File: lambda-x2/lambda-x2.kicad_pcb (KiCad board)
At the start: 4 copper layers, 81.8 x 100.9 mm, 263 parts, among them J1 FTSH-107-01-F-DV-K, J3 Conn_02x02_Odd_Even, J4 Conn_01x10, P1 33311-24AW-2, Q1 BTS3028, Q2 BTS3028, Q3 BTS3028, Q4 BTS3028, U1 MAX31855KASA, U10 MCP6002T-I/SN, U11 GS8332-SR, U12 MCP6002T-I/SN, U13 MCP6002T-I/SN, U14 MAX31855KASA, U15 MAX31856, U16 MAX31856, U17 MCP6002T-I/SN, U18 JDY-33, U2 STM32F103C6Tx, U3 MCP6002T-I/SN, U4 LM78M05_TO252, U5 XC6206P332MR, U6 REF3033, U7 MCP6002T-I/SN, U8 TJA1051T-3, U9 GS8332-SR, Y1 XXDCELNANF-8MHZ

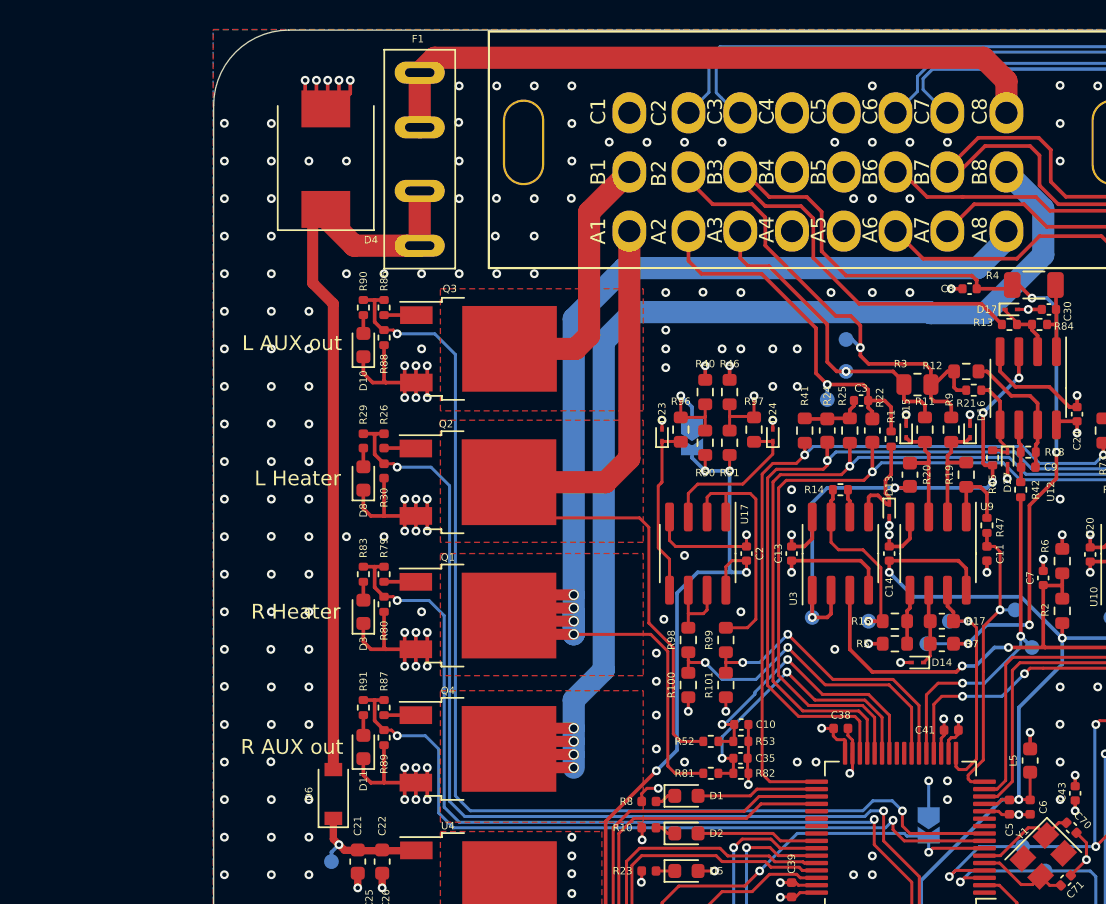
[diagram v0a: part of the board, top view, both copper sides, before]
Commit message: lambda-x2: fuse, Vbat sense, resistor in sense
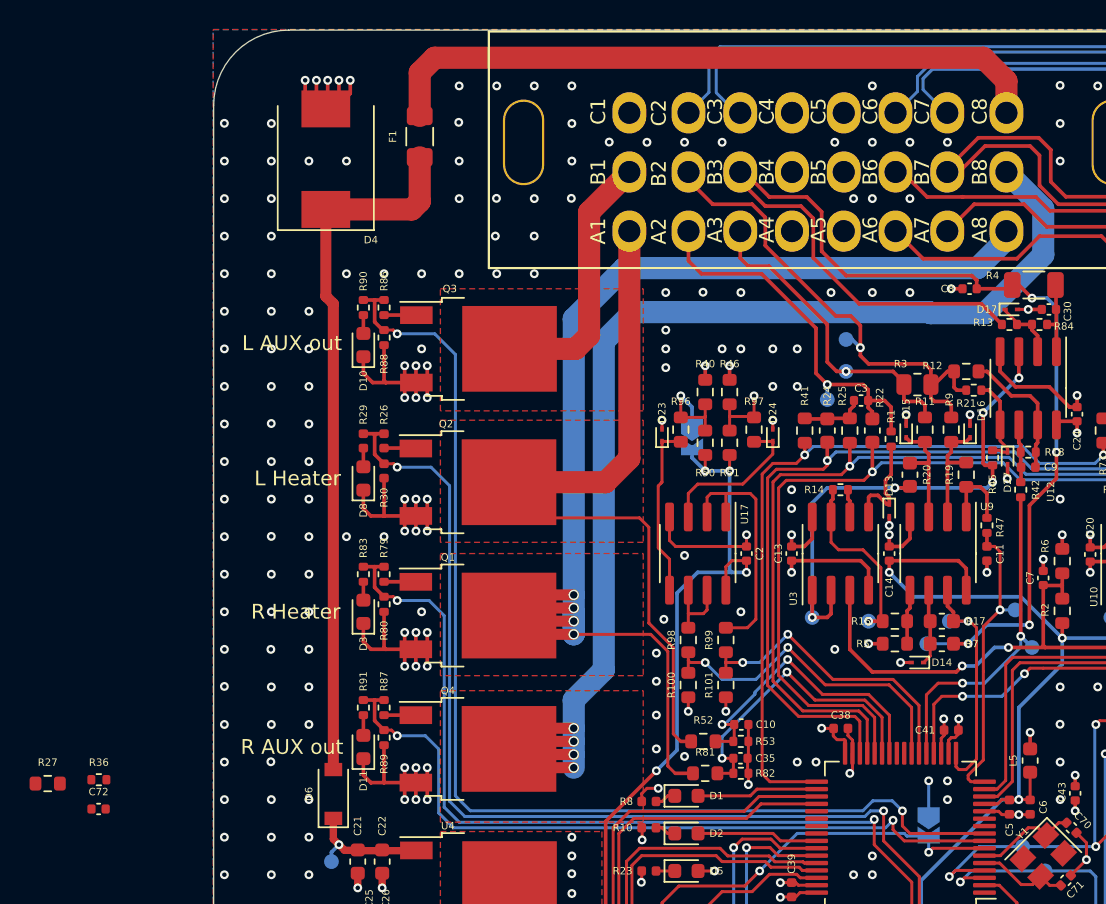
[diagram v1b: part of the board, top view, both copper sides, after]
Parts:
- added C72: 1n, Capacitor_SMD:C_0402_1005Metric, F.Cu at (84.8, 84.5)
- added R27: 100k 1%, Resistor_SMD:R_0603_1608Metric, F.Cu at (81.4, 82.7)
- added R36: 10k 1%, Resistor_SMD:R_0402_1005Metric, F.Cu at (84.9, 82.5)
- C10, C35: value 100n -> 1n
- D5: value WHITE -> GREEN
- F1: value XF-506P -> BSMD1206-025-33V; footprint wideband_controller:XF-506P -> Fuse:Fuse_1206_3216Metric
- R52, R81: footprint Resistor_SMD:R_0402_1005Metric -> Resistor_SMD:R_0603_1608Metric
- moved F1 1.52 mm to (106.6, 39.0)
- moved R52 0.51 mm to (125.7, 79.9)
- moved R81 0.38 mm to (125.9, 82.0)
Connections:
- net 12V_PROT renamed Net-(D4-Pad1)
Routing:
- net Net-(D4-Pad1): track 50.2 -> 47.6 mm
- net /L_LSU_Heater-: track 51.8 -> 51.0 mm
- net 12V_RAW: track 46.6 -> 45.8 mm
- net /R_LSU_Heater-: track 92.1 -> 91.4 mm

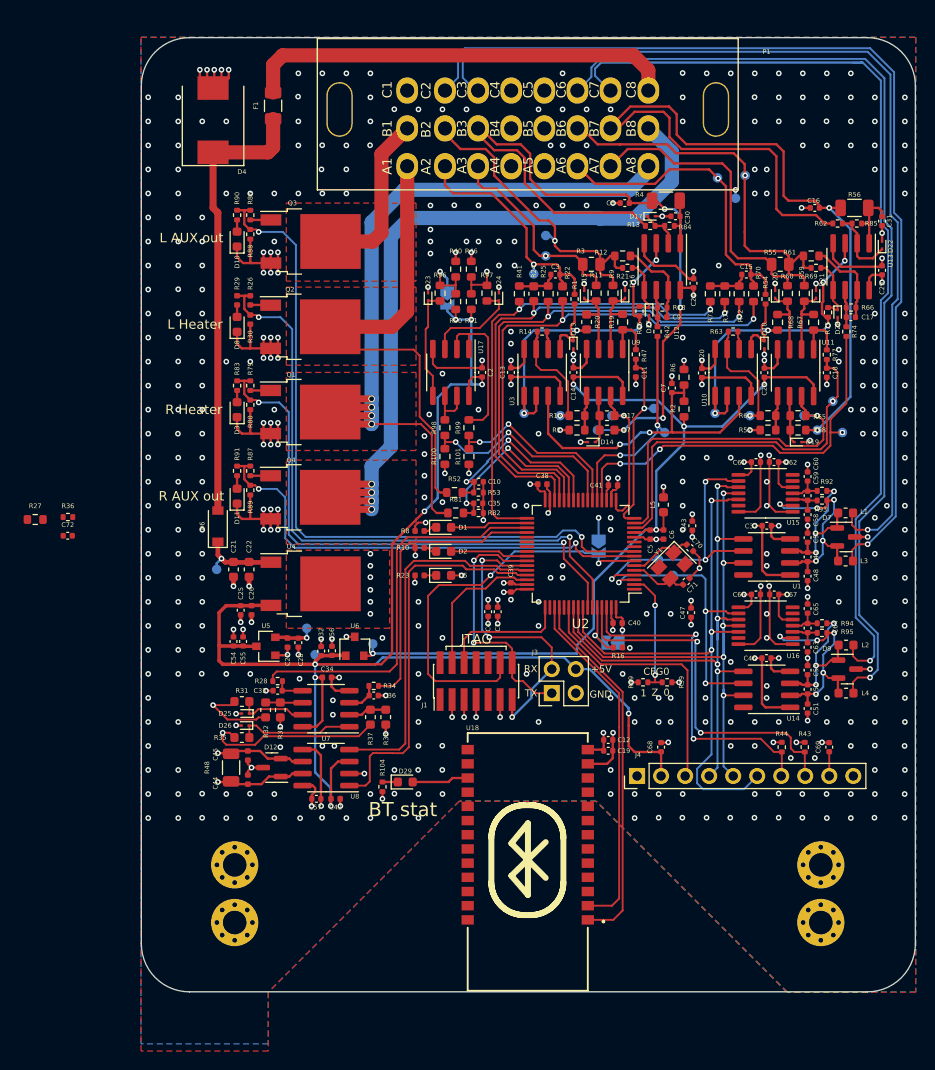
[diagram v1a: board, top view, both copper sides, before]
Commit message: lambda-x2: diagnostic for AUX out, PWM noise cancelation, etc
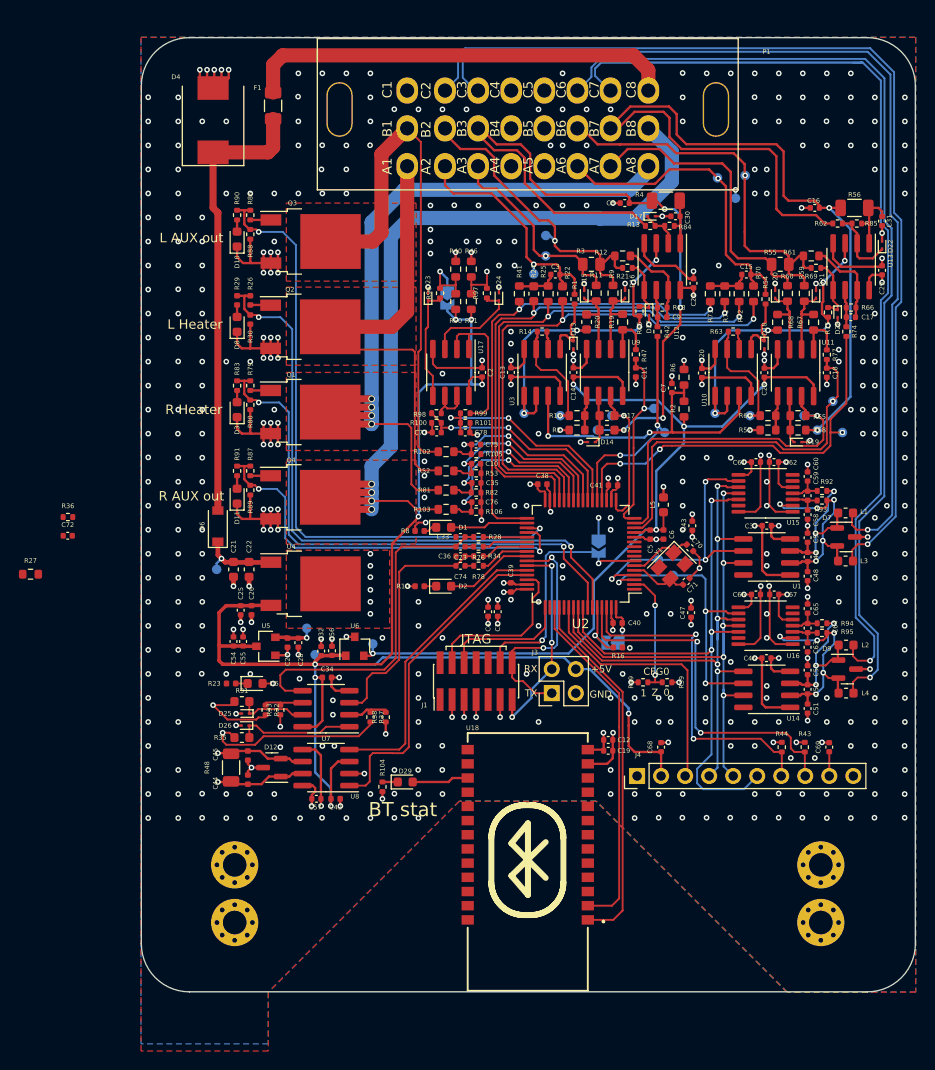
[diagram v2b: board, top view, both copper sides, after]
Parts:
- added C73: 100n, Capacitor_SMD:C_0402_1005Metric, F.Cu at (126.4, 85.6)
- added C74: 100n, Capacitor_SMD:C_0402_1005Metric, F.Cu at (126.4, 87.6)
- added C75: 1n, Capacitor_SMD:C_0402_1005Metric, F.Cu at (128.0, 74.8)
- added C76: 1n, Capacitor_SMD:C_0402_1005Metric, F.Cu at (128.0, 80.9)
- added C77: 1n, Capacitor_SMD:C_0402_1005Metric, F.Cu at (123.9, 73.5)
- added C78: 1n, Capacitor_SMD:C_0402_1005Metric, F.Cu at (126.9, 73.5)
- added R102: 100k 1%, Resistor_SMD:R_0603_1608Metric, F.Cu at (124.8, 75.6)
- added R103: 100k 1%, Resistor_SMD:R_0603_1608Metric, F.Cu at (124.8, 81.7)
- added R105: 10k 1%, Resistor_SMD:R_0402_1005Metric, F.Cu at (128.0, 75.8)
- added R106: 10k 1%, Resistor_SMD:R_0402_1005Metric, F.Cu at (128.0, 81.9)
- added R76: 3.3k, Resistor_SMD:R_0402_1005Metric, F.Cu at (128.3, 85.6)
- added R78: 3.3k, Resistor_SMD:R_0402_1005Metric, F.Cu at (128.3, 87.6)
- C33, C36: value 2.2u -> 100n
- R100, R101, R32, R33, R37, R38, R98, R99: footprint Resistor_SMD:R_0603_1608Metric -> Resistor_SMD:R_0402_1005Metric
- R96, R97: value 10k 0.1% -> 10k; footprint Resistor_SMD:R_0603_1608Metric -> Resistor_SMD:R_0402_1005Metric
- moved R28 26.1 mm to (128.3, 84.6), turned to 180 degrees
- moved C33 25.3 mm to (126.4, 84.6)
- moved D5 23.0 mm to (104.6, 100.1)
- moved R23 23.0 mm to (102.1, 100.1)
- moved R34 17.6 mm to (128.3, 86.6)
- moved C36 17.4 mm to (126.4, 86.6), turned to 180 degrees
- moved R27 5.81 mm to (80.9, 88.5)
- moved R10 4.06 mm to (122.0, 89.8)
- moved D2 3.68 mm to (124.6, 89.8)
- moved R100 3.67 mm to (123.8, 72.5), turned to 0 degrees
- moved R101 3.58 mm to (126.9, 72.5), turned to 180 degrees
- moved R81 2.62 mm to (124.8, 79.6)
- moved R52 2.45 mm to (124.8, 77.6)
- moved R82 2.17 mm to (128.0, 79.9)
- moved C35 2.17 mm to (128.1, 78.9)
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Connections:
- net Net-(C33-Pad1) renamed /DACout1
- net Net-(C36-Pad1) renamed /DACout2
- R28 pad 1: /PWMout1 -> Net-(U2-Pad37)
- R34 pad 1: /PWMout2 -> Net-(U2-Pad39)
- R96 pad 1: Net-(D23-Pad1) -> /L_AUX
- R96 pad 2: /L_AUX -> Net-(D23-Pad1)
- R97 pad 1: Net-(D24-Pad1) -> /R_AUX
- R97 pad 2: /R_AUX -> Net-(D24-Pad1)
- U2 pad 24: unconnected-(U2-Pad24) -> /L_OUT_sense
- U2 pad 25: unconnected-(U2-Pad25) -> /L_Heater_sense
- U2 pad 26: /L_Heater_sense -> /R_Heater_sense
- U2 pad 27: /R_Heater_sense -> /R_OUT_sense
- U2 pad 35: /PWMout1 -> /L_OUT_en
- U2 pad 36: /PWMout2 -> /R_OUT_en
- U2 pad 37: unconnected-(U2-Pad37) -> Net-(U2-Pad37)
- U2 pad 38: unconnected-(U2-Pad38) -> Net-(U2-Pad38)
- U2 pad 39: unconnected-(U2-Pad39) -> Net-(U2-Pad39)
- U2 pad 40: unconnected-(U2-Pad40) -> Net-(U2-Pad40)
- U2 pad 8: /R_OUT_en -> unconnected-(U2-Pad8)
- U2 pad 9: /L_OUT_en -> unconnected-(U2-Pad9)
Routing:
- net /PWMout1: track 41.2 -> 0.00 mm
- net /L_OD: track 17.9 -> 54.6 mm
- net /DACout1: track 3.08 -> 36.8 mm
- net /PWMout2: track 30.3 -> 0.00 mm
- net /DACout2: track 3.34 -> 26.2 mm
- net /R_OUT_sense: track 0.00 -> 21.4 mm, vias 0 -> 2
- net /L_OUT_sense: track 0.00 -> 21.1 mm, vias 0 -> 2
- net /nRESET: track 42.9 -> 26.2 mm
- net /L_OUT_en: track 77.1 -> 67.1 mm
- net /UART_RX: track 31.4 -> 22.2 mm
- net /R_OUT_en: track 50.7 -> 42.9 mm
- net /R_OD: track 87.5 -> 94.9 mm
- net /CAN_RX: track 38.2 -> 31.7 mm
- net /CAN_TX: track 41.3 -> 34.7 mm
- net Net-(U2-Pad40): track 0.00 -> 5.24 mm
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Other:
- board text removed: "FUSE"

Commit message: lambda-x2: jtag, adc channels, one more led, BT en, etc
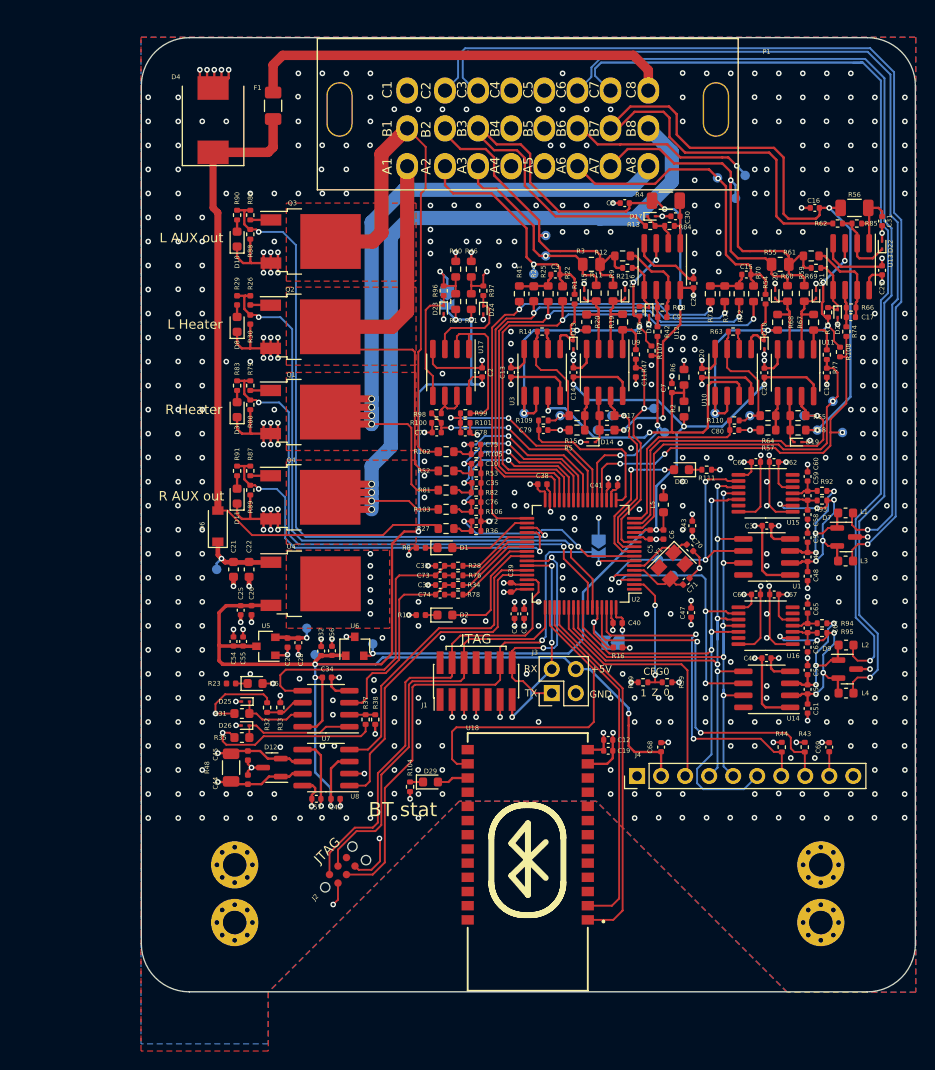
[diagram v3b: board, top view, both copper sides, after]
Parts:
- added C79: 1n, Capacitor_SMD:C_0402_1005Metric, F.Cu at (135.1, 73.3)
- added C80: 1n, Capacitor_SMD:C_0402_1005Metric, F.Cu at (155.3, 73.3)
- added D30: GREEN, LED_SMD:LED_0603_1608Metric, F.Cu at (149.7, 77.5)
- added J2: tc2030-idc-nl, rusefi:tc2030-idc-nl, F.Cu at (112.1, 121.6)
- added R107: 10k, Resistor_SMD:R_0402_1005Metric, F.Cu at (146.6, 64.9)
- added R108: 10k, Resistor_SMD:R_0402_1005Metric, F.Cu at (166.5, 65.0)
- added R109: 1k, Resistor_SMD:R_0402_1005Metric, F.Cu at (135.1, 72.3)
- added R110: 1k, Resistor_SMD:R_0402_1005Metric, F.Cu at (155.3, 72.3)
- added R111: 1k, Resistor_SMD:R_0402_1005Metric, F.Cu at (152.4, 77.5)
- R15, R64: value 10k 0.1% -> 2.7k 0.1%
- R5, R57: value 30k 1% -> 10k 0.1%
- moved R27 44.2 mm to (124.8, 83.7)
- moved C72 43.2 mm to (128.0, 82.9)
- moved R36 43.2 mm to (128.0, 83.9), turned to 180 degrees
- moved R28 3.73 mm to (126.1, 87.6)
- moved R34 3.73 mm to (126.1, 89.7)
- moved R76 3.73 mm to (126.1, 88.6)
- moved C33 3.73 mm to (124.2, 87.6)
- moved C36 3.73 mm to (124.2, 89.7)
- moved C73 3.73 mm to (124.2, 88.6)
- moved C74 3.73 mm to (124.2, 90.7)
- moved R78 3.73 mm to (126.1, 90.7)
- moved R10 3.05 mm to (122.2, 92.8)
- moved D2 3.05 mm to (124.7, 92.8)
- moved R104 2.92 mm to (121.0, 111.0)
- moved C1 2.80 mm to (133.1, 92.7)
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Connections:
- net /LED_GREEN renamed /L_LED_GREEN
- U18 pad 15: unconnected-(U18-Pad15) -> /BT_EN
- U2 pad 10: unconnected-(U2-Pad10) -> /L_Un_3x_sense
- U2 pad 11: unconnected-(U2-Pad11) -> /L_Ip_sense
- U2 pad 16: /L_Ip_sense -> /R_Un_sense
- U2 pad 17: /L_Un_3x_sense -> /L_Un_sense
- U2 pad 50: unconnected-(U2-Pad50) -> /BT_EN
- U2 pad 8: unconnected-(U2-Pad8) -> /12V_sense
- U2 pad 9: unconnected-(U2-Pad9) -> /R_LED_GREEN
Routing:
- net /nRESET: track 26.2 -> 62.0 mm
- net /BT_EN: track 0.00 -> 34.2 mm
- net /SWDIO: track 17.4 -> 49.0 mm
- net /SWCLK: track 13.4 -> 44.6 mm
- net Net-(D4-Pad1): track 47.6 -> 72.6 mm
- net /12V_sense: track 0.00 -> 23.7 mm, vias 0 -> 2
- net /R_Un_sense: track 0.00 -> 19.2 mm
- net /L_Un_sense: track 0.00 -> 17.5 mm
- net /R_LED_GREEN: track 0.00 -> 15.5 mm, vias 0 -> 2
- net GND: track 279.1 -> 293.6 mm, vias 458 -> 510
- net /DACout2: track 26.2 -> 21.1 mm
- net /DACout1: track 36.8 -> 31.7 mm
- net /L_Un_3x_sense: track 16.8 -> 21.3 mm
- net /L_Ip_sense: track 20.4 -> 23.8 mm
- net Net-(R78-Pad1): track 5.24 -> 8.66 mm
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
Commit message: lambda-x2: update PCB dimentions, connector footprint, etx
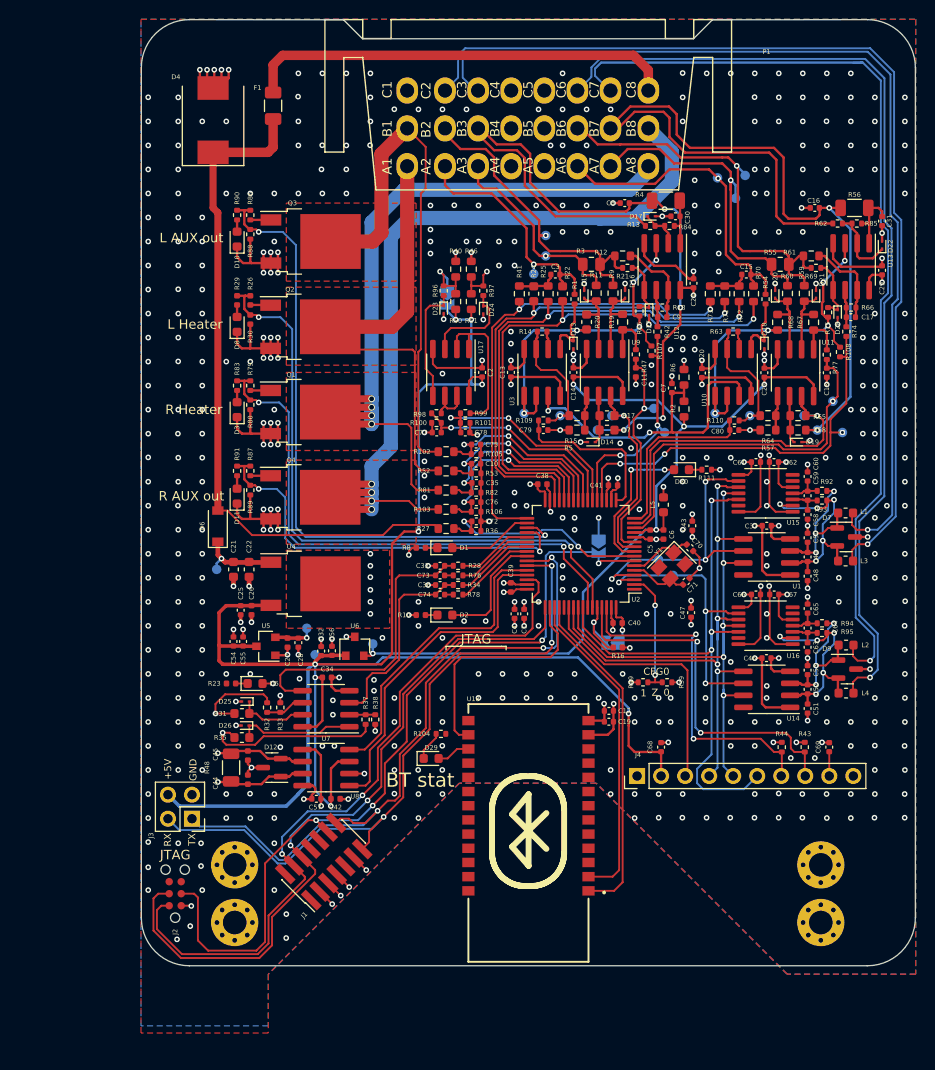
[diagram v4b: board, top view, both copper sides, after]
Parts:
- moved J3 40.3 mm to (98.0, 114.4), turned to 180 degrees
- moved J1 25.0 mm to (111.9, 118.9), turned to 135 degrees
- moved J2 16.2 mm to (96.2, 124.8), turned to 90 degrees
- moved R104 6.48 mm to (124.3, 105.4), turned to 180 degrees
- moved C12 3.07 mm to (142.1, 103.0)
- moved C19 3.07 mm to (142.1, 104.1)
- moved U18 3.07 mm to (133.6, 115.7)
- moved D29 2.49 mm to (123.3, 108.0)
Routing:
- net /UART_RX: track 22.2 -> 73.0 mm
- net /UART_TX: track 25.0 -> 72.8 mm, vias 2 -> 3
- net /SWCLK: track 44.6 -> 76.7 mm, vias 0 -> 2
- net +5V: track 167.7 -> 197.1 mm
- net /SWDIO: track 49.0 -> 76.9 mm, vias 0 -> 2
- net /nRESET: track 62.0 -> 88.1 mm, vias 2 -> 4
- net /BT_EN: track 34.2 -> 25.0 mm
- net GND: track 293.6 -> 286.9 mm, vias 510 -> 521
- net /BT_UART_TX: track 37.2 -> 34.1 mm
- net /BT_UART_RX: track 38.9 -> 35.8 mm
- net Net-(D29-Pad1): track 1.37 -> 3.14 mm
- net +3V3: track 82.8 -> 81.3 mm
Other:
- board size 81.8 x 100.9 mm -> 81.8 x 100 mm
